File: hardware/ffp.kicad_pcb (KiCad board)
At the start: 2 copper layers, 40.8 x 10.6 mm, 17 parts, among them IC1 STM32F042K6T7, IC2 MCP1700, IC3 MIC2004-0_5YM5, J2 USB_C_Receptacle_USB2.0, J3 PROG, P1 SWD_TC

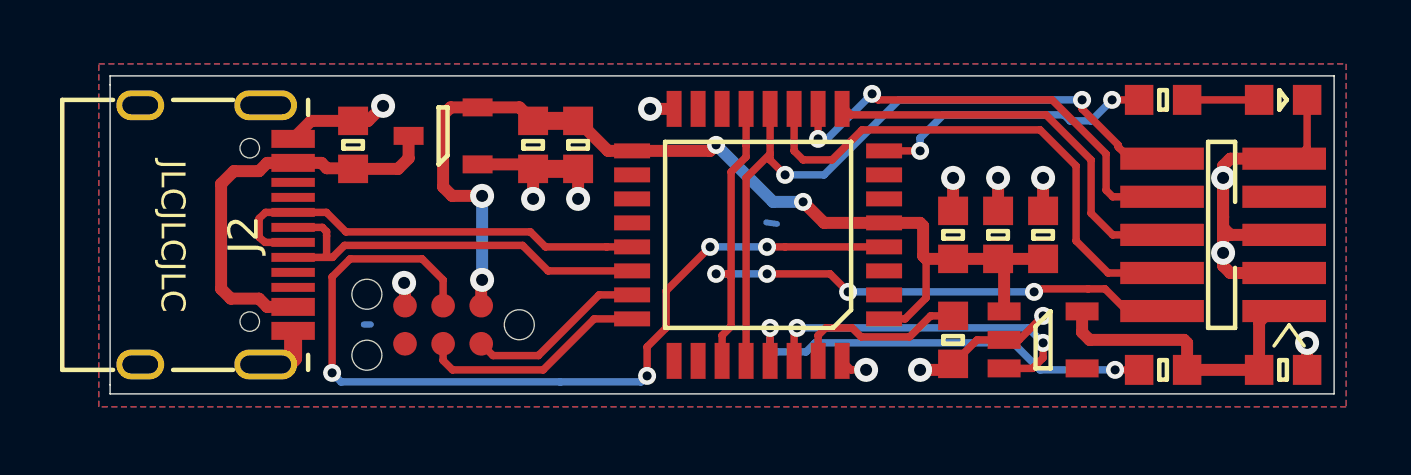
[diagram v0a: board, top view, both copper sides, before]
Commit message: adjust the border and remove the top copper
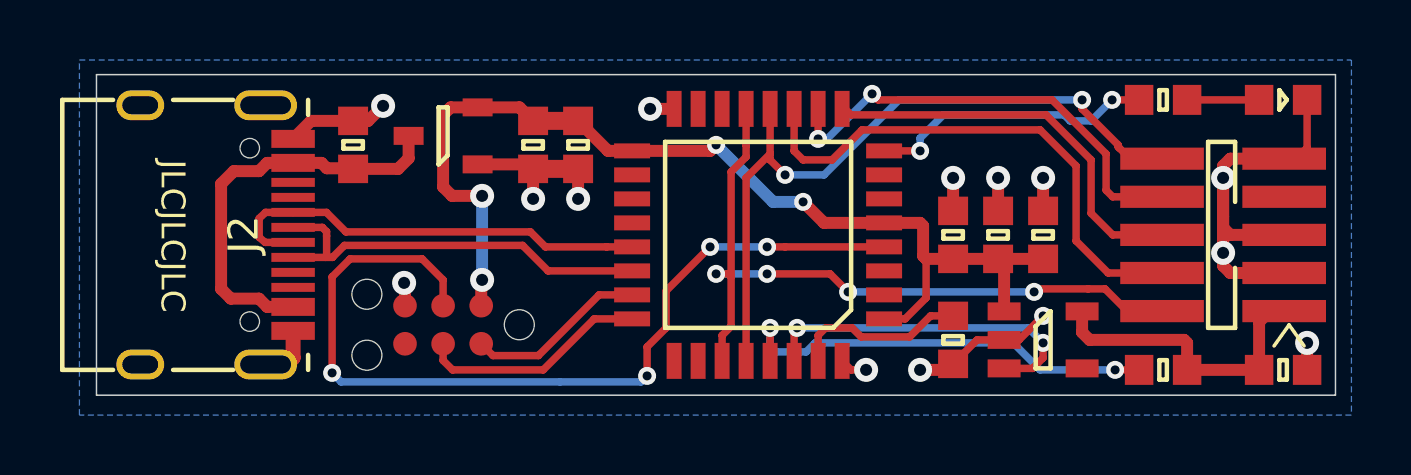
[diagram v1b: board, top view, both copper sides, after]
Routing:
- net GND: track 37.7 -> 37.1 mm
- removed copper zone on F.Cu, net GND
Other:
- board size 40.8 x 10.6 mm -> 41.3 x 10.7 mm
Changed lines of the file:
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@@
   (general
     (thickness 1.6)
-    (drawings 12)
-    (tracks 274)
+    (drawings 8)
+    (tracks 272)
     (zones 0)
     (modules 17)
@@
   )
   (setup
-    (last_trace_width 0.25)
+    (last_trace_width 0.2)
     (user_trace_width 0.2)
     (user_trace_width 0.25)
@@
     (user_trace_width 0.6)
     (trace_clearance 0.2)
-    (zone_clearance 0.508)
+    (zone_clearance 0.275)
     (zone_45_only no)
     (trace_min 0.2)
@@
   (gr_line (start 152.2 123) (end 152.7 123.7) (layer F.SilkS) (width 0.12))
   (gr_line (start 151.7 123.7) (end 152.2 123) (layer F.SilkS) (width 0.12))
-  (dimension 10.6 (width 0.15) (layer F.Fab)
-    (gr_text "10.600 mm" (at 158.4 120 270) (layer F.Fab)
-      (effects (font (size 1 1) (thickness 0.15)))
-    )
-    (feature1 (pts (xy 153.7 125.3) (xy 157.686421 125.3)))
-    (feature2 (pts (xy 153.7 114.7) (xy 157.686421 114.7)))
-    (crossbar (pts (xy 157.1 114.7) (xy 157.1 125.3)))
-    (arrow1a (pts (xy 157.1 125.3) (xy 156.513579 124.173496)))
-    (arrow1b (pts (xy 157.1 125.3) (xy 157.686421 124.173496)))
-    (arrow2a (pts (xy 157.1 114.7) (xy 156.513579 115.826504)))
-    (arrow2b (pts (xy 157.1 114.7) (xy 157.686421 115.826504)))
-  )
-  (dimension 40.8 (width 0.15) (layer F.Fab)
-    (gr_text "40.800 mm" (at 133.3 130.2) (layer F.Fab)
-      (effects (font (size 1 1) (thickness 0.15)))
-    )
-    (feature1 (pts (xy 112.9 125.3) (xy 112.9 129.486421)))
-    (feature2 (pts (xy 153.7 125.3) (xy 153.7 129.486421)))
-    (crossbar (pts (xy 153.7 128.9) (xy 112.9 128.9)))
-    (arrow1a (pts (xy 112.9 128.9) (xy 114.026504 128.313579)))
-    (arrow1b (pts (xy 112.9 128.9) (xy 114.026504 129.486421)))
-    (arrow2a (pts (xy 153.7 128.9) (xy 152.573496 128.313579)))
-    (arrow2b (pts (xy 153.7 128.9) (xy 152.573496 129.486421)))
-  )
-  (gr_line (start 153.7 114.7) (end 153.7 125.3) (layer Edge.Cuts) (width 0.05))
-  (gr_line (start 112.9 125.3) (end 112.9 125) (layer Edge.Cuts) (width 0.05))
-  (gr_line (start 153.7 125.3) (end 112.9 125.3) (layer Edge.Cuts) (width 0.05))
-  (gr_line (start 112.9 114.7) (end 112.9 115) (layer Edge.Cuts) (width 0.05))
-  (gr_line (start 153.7 114.7) (end 112.9 114.7) (layer Edge.Cuts) (width 0.05))
-  (gr_line (start 112.9 115) (end 112.9 125) (layer Edge.Cuts) (width 0.05))
-  (segment (start 121.3612 122.9868) (end 121.5898 122.9868) (width 0.21) (layer B.Cu) (net 1))
-  (segment (start 134.7724 119.5832) (end 135.128 119.634) (width 0.2) (layer B.Cu) (net 1))
+  (gr_line (start 153.7462 114.65814) (end 153.7462 125.34392) (layer Edge.Cuts) (width 0.05))
+  (gr_line (start 153.7462 125.34392) (end 112.4458 125.34392) (layer Edge.Cuts) (width 0.05))
+  (gr_line (start 153.7462 114.65814) (end 112.4458 114.65814) (layer Edge.Cuts) (width 0.05))
+  (gr_line (start 112.4458 114.65814) (end 112.4458 125.34392) (layer Edge.Cuts) (width 0.05))
   (segment (start 127 117.8) (end 128.5 117.8) (width 0.6) (layer F.Cu) (net 1))
   (via (at 138.1 124.5) (size 0.8) (drill 0.4) (layers F.Cu B.Cu) (net 1))
@@
   (segment (start 119.6 116.2) (end 119 116.8) (width 0.4) (layer F.Cu) (net 1))
   (segment (start 121 116.2) (end 119.6 116.2) (width 0.4) (layer F.Cu) (net 1))
-  (segment (start 119 124.1) (end 119 123.2) (width 0.6) (layer F.Cu) (net 1))
-  (segment (start 118.78 124.32) (end 119 124.1) (width 0.6) (layer F.Cu) (net 1))
+  (segment (start 119 124.1) (end 119 123.2) (width 0.5) (layer F.Cu) (net 1))
+  (segment (start 118.78 124.32) (end 119 124.1) (width 0.5) (layer F.Cu) (net 1))
   (segment (start 118.085 124.32) (end 118.78 124.32) (width 0.6) (layer F.Cu) (net 1))
   (segment (start 127 116.2) (end 128.5 116.2) (width 0.6) (layer F.Cu) (net 2))
@@
   (segment (start 151.2 115.5) (end 148.8 115.5) (width 0.25) (layer F.Cu) (net 37))
   (zone (net 1) (net_name GND) (layer B.Cu) (hatch edge 0.508)
-    (connect_pads (clearance 0.4))
-    (min_thickness 0.254)
-    (fill yes (arc_segments 32) (thermal_gap 0.4) (thermal_bridge_width 0.4))
+    (connect_pads (clearance 0.275))
+    (min_thickness 0.27)
+    (fill yes (arc_segments 32) (thermal_gap 0.275) (thermal_bridge_width 0.275))
     (polygon
       (pts
-        (xy 112.522 114.3) (xy 154.1018 114.3) (xy 154.1018 125.73) (xy 112.522 125.73)
+        (xy 111.87684 114.17046) (xy 154.27706 114.17046) (xy 154.27706 126.00686) (xy 111.87684 126.00686)
       )
     )
-  )
-  (zone (net 1) (net_name GND) (layer F.Cu) (hatch edge 0.508)
-    (connect_pads (clearance 0.4))
-    (min_thickness 0.254)
-    (fill yes (arc_segments 32) (thermal_gap 0.4) (thermal_bridge_width 0.4))
-    (polygon
-      (pts
-        (xy 112.522 114.3) (xy 154.1018 114.3) (xy 154.1018 125.73) (xy 112.522 125.73)
-      )
-    )
